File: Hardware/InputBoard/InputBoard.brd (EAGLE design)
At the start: 41.9 x 30.1 mm, 8 parts, among them IC1 LM358N

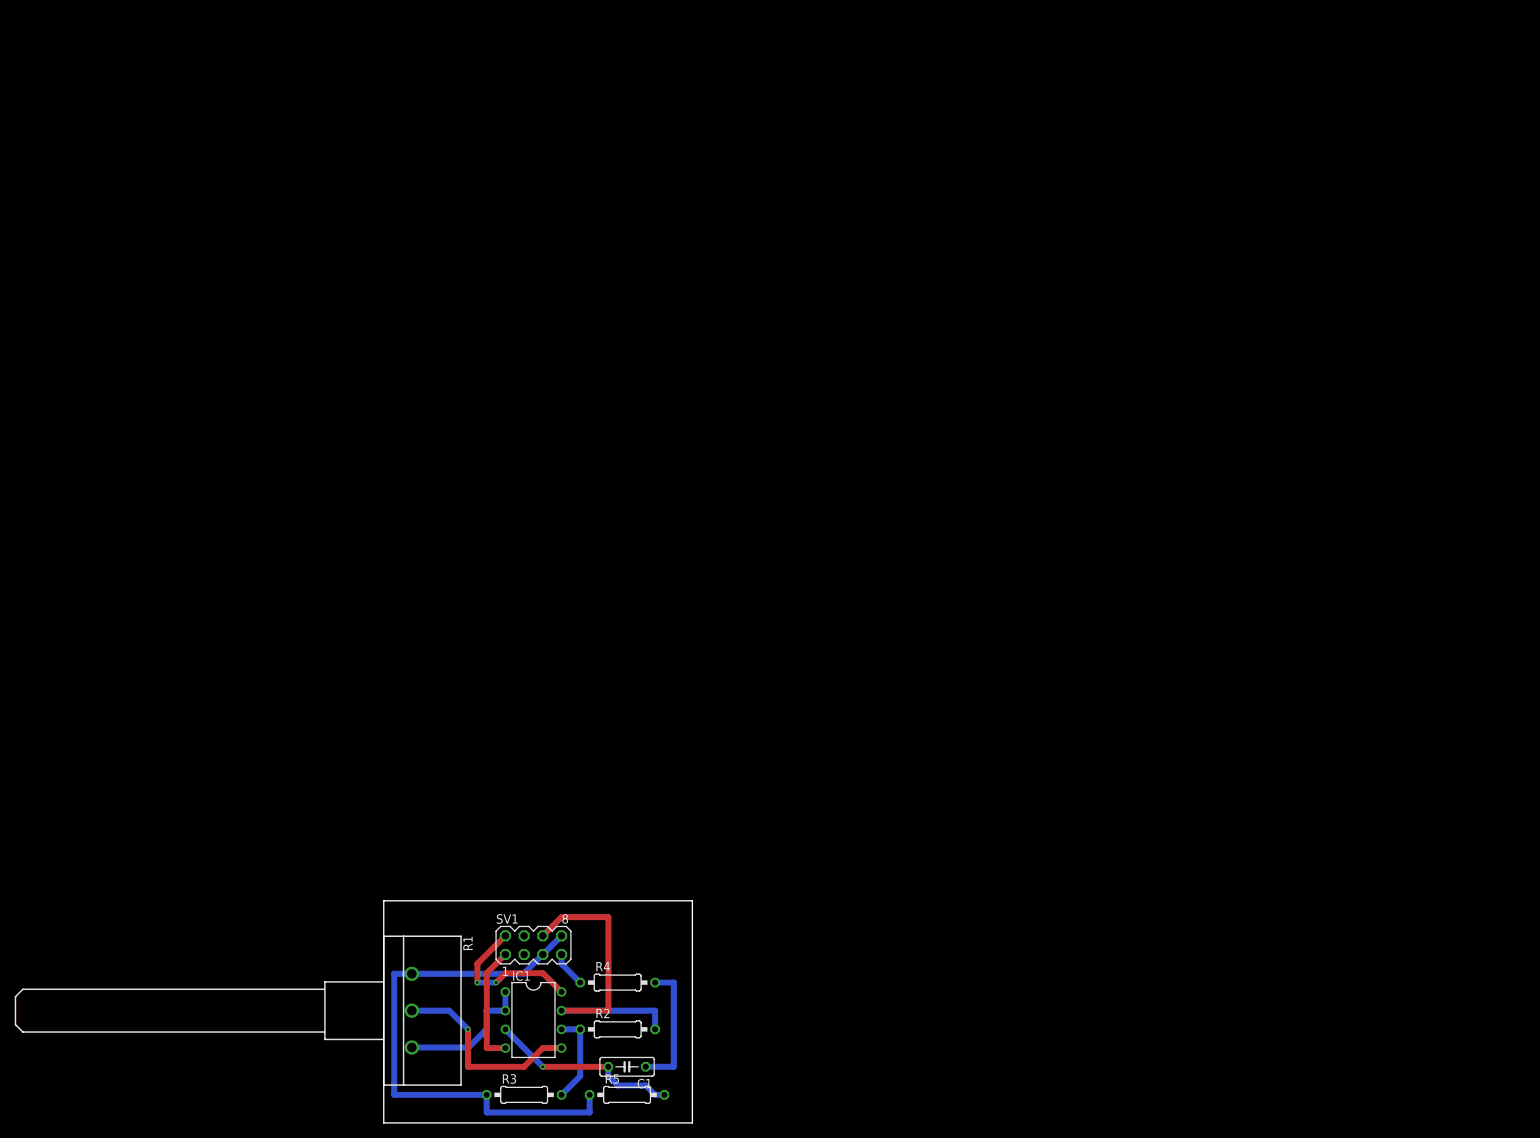
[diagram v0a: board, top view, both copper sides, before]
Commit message: InputBoard überarbeitet, pinout bereitgestellt
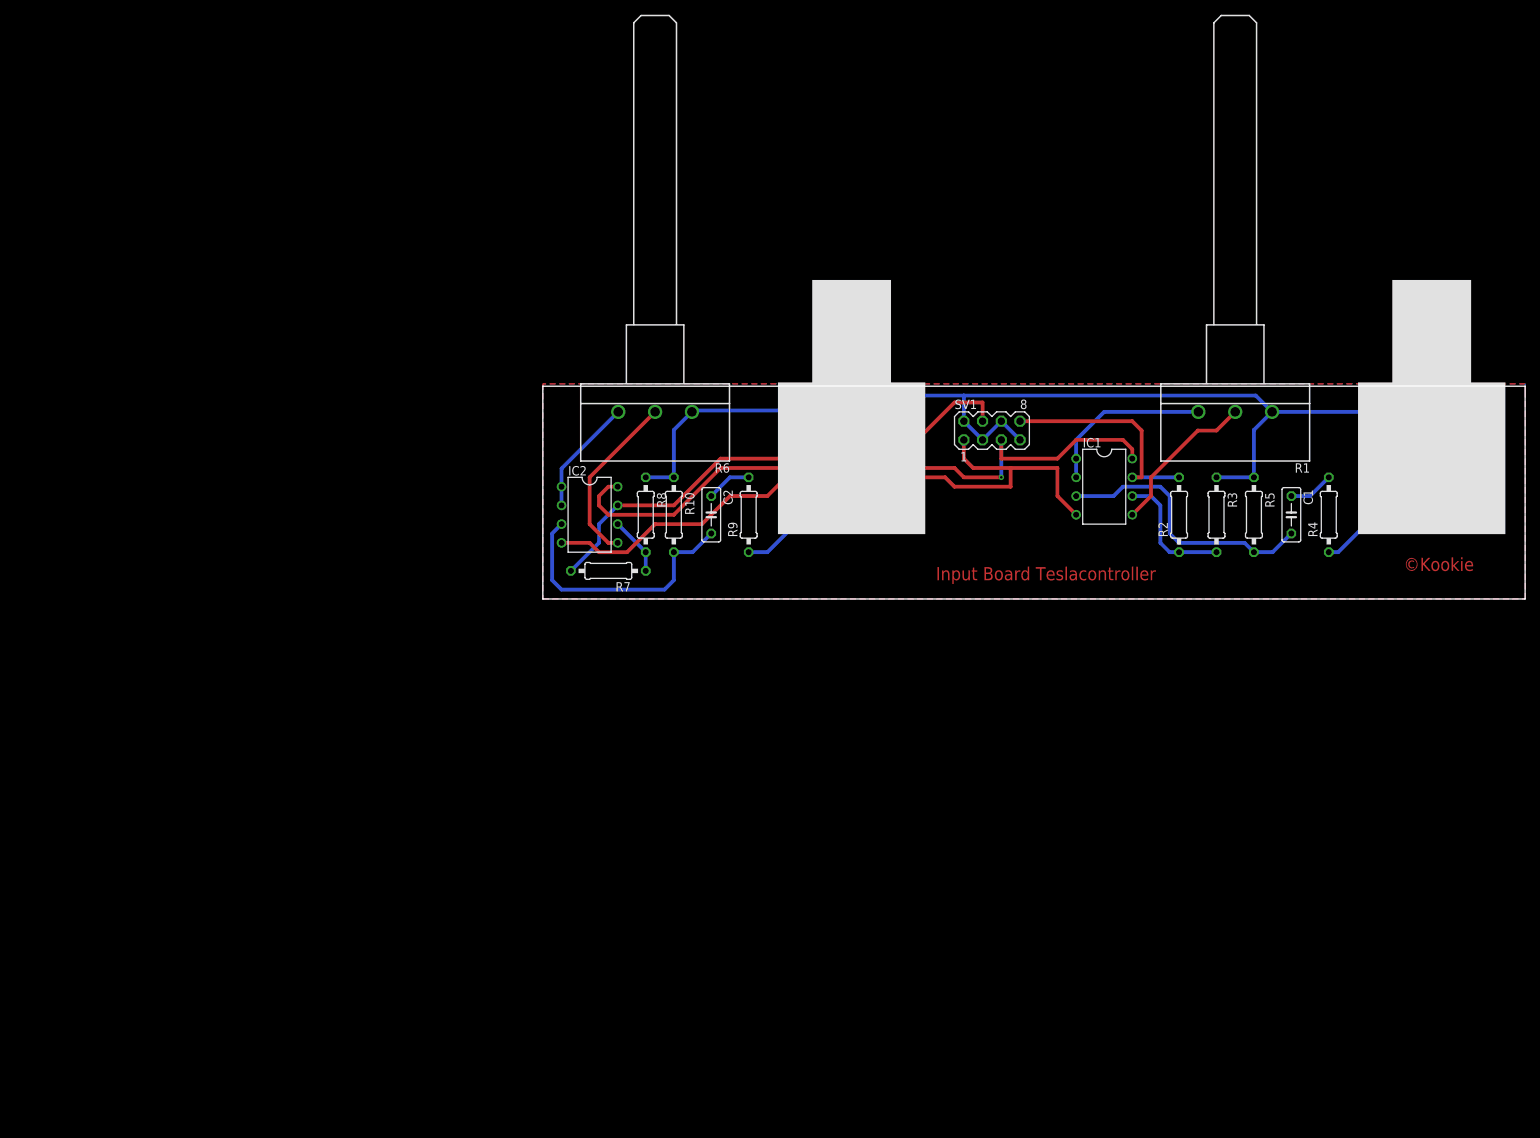
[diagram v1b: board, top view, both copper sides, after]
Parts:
- added C2: 0.001u, rcl:C050-025X075
- added IC2: LM358N, linear:DIL08
- added R10: 1M8, rcl:0207/10
- added R6: (no value), pot:CIP20C-6MM
- added R7: 200k, rcl:0207/10
- added R8: 10k, rcl:0207/10
- added R9: 100k, rcl:0207/10
- added U$1, U$2: (no value), EBS63P:EBS63P
- moved R1 138.2 mm to (115.6, 96.5), turned to 180 degrees
- moved R3 122.6 mm to (113.0, 82.5), turned to 270 degrees
- moved C1 117.2 mm to (123.2, 82.5), turned to 270 degrees
- moved R5 115.9 mm to (118.1, 82.5), turned to 270 degrees
- moved R4 115.5 mm to (128.3, 82.5), turned to 90 degrees
- moved IC1 106.0 mm to (97.8, 86.4)
- moved R2 103.4 mm to (108.0, 82.5), turned to 90 degrees
- moved SV1 93.5 mm to (82.5, 94.0)
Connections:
- removed net IN: R4.1, SV1.7
- removed net OUT: IC1.7, R2.2, SV1.6
- new net N$10: C2.1, R9.2
- new net N$11: R9.1, U$2.P$2
- new net N$12: R4.1, U$1.P$2
- new net N$6: IC2.1, IC2.2, R6.E
- new net N$7: IC2.5, R6.S
- new net N$8: IC2.6, R7.1, R8.2
- new net N$9: C2.2, IC2.3, R10.2
- new net OUT1: IC1.7, R2.2, SV1.8
- new net OUT2: IC2.7, R7.2, SV1.4
- net GND: now also R10.1, R6.A, R8.1, SV1.2, SV1.3, SV1.6, SV1.7, U$1.P$1, U$2.P$1; no longer SV1.5, SV1.8
- net V+: now also IC2.8, SV1.5; no longer SV1.2
- net V-: now also IC2.4
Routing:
- net V-: track 16.3 -> 91.9 mm
- net V+: track 20.9 -> 90.9 mm, vias 2 -> 1
- net OUT2: track 0.00 -> 69.4 mm
- net GND: track 72.6 -> 137.5 mm
- net OUT: track 44.2 -> 0.00 mm
- net N$9: track 0.00 -> 35.7 mm
- net OUT1: track 0.00 -> 31.0 mm
- net N$7: track 0.00 -> 23.8 mm
- net N$6: track 0.00 -> 15.9 mm
- net N$5: track 17.8 -> 6.13 mm
- net N$4: track 26.0 -> 37.4 mm, vias 1 -> 0
- net N$11: track 0.00 -> 10.8 mm
- net N$12: track 0.00 -> 9.77 mm
- net N$8: track 0.00 -> 7.93 mm
- net N$2: track 27.5 -> 21.2 mm, vias 1 -> 0
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- added copper zone on layer 1, net GND
- added copper zone on layer 16, net GND
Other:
- board size 41.9 x 30.1 mm -> 133.3 x 28.9 mm
- board text added: "Input Board Teslacontroller"
- board text added: "©Kookie"

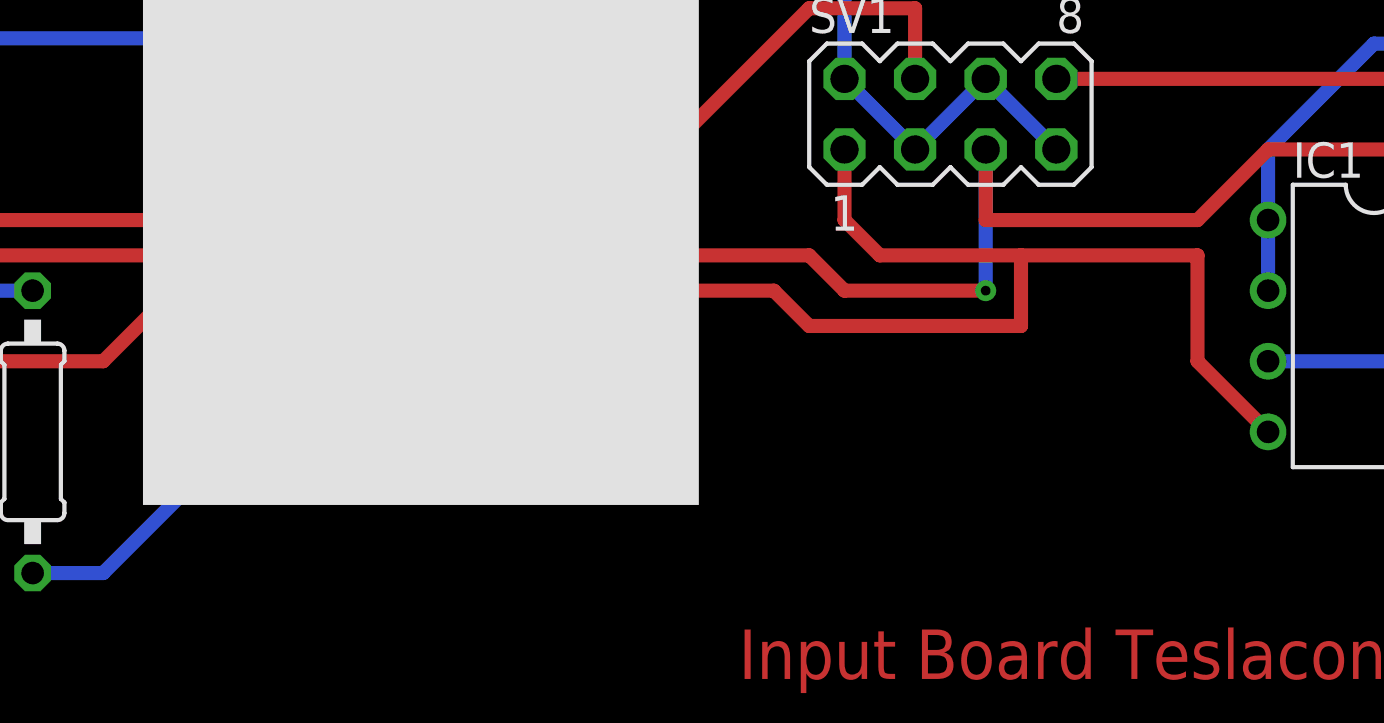
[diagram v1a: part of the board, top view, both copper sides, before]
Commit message: Letzte Änderungen an Netzteil, OP und IP Board
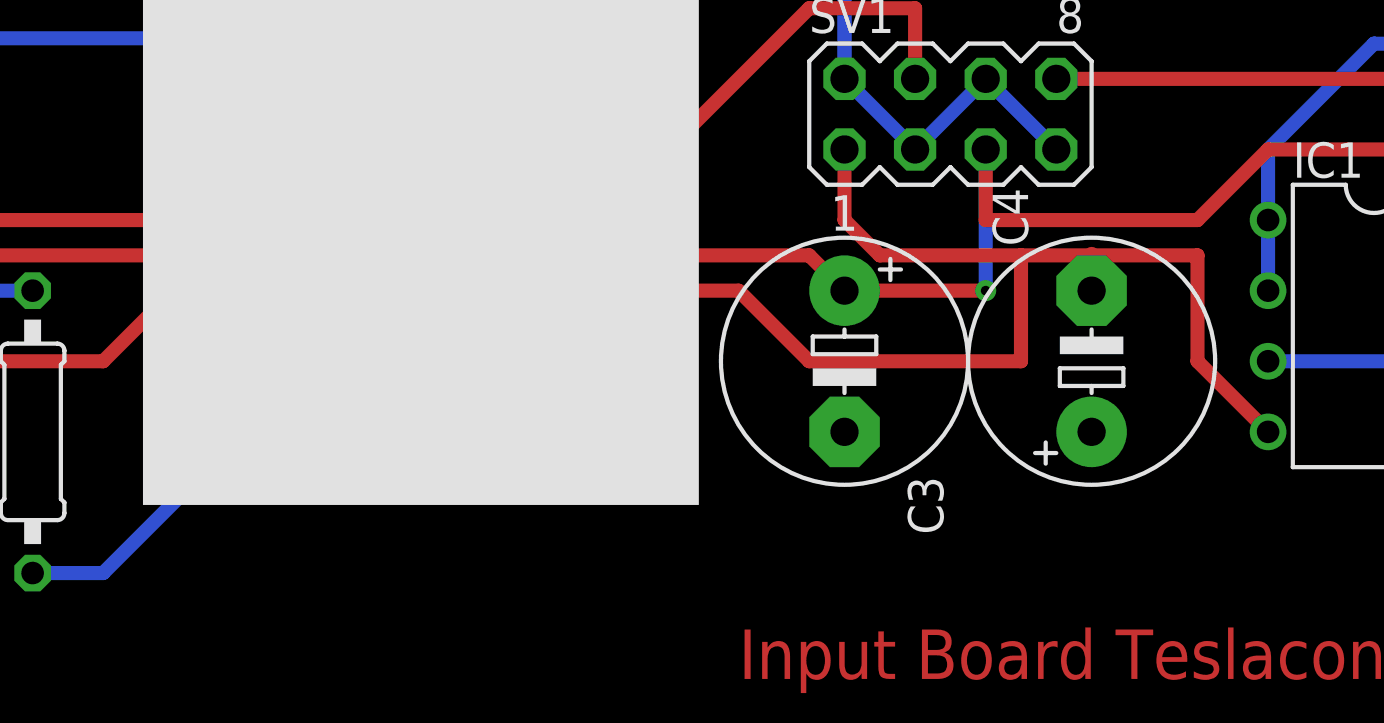
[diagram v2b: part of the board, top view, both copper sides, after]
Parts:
- added C3, C4: (no value), rcl:E5-8,5
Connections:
- net GND: now also C3.-, C4.+
- net V+: now also C3.+
- net V-: now also C4.-
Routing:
- net V-: track 91.9 -> 95.0 mm
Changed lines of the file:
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@@
 <?xml version="1.0" encoding="utf-8"?>
 <!DOCTYPE eagle SYSTEM "eagle.dtd">
-<eagle version="9.4.1">
+<eagle version="9.4.0">
 <drawing>
 <settings>
@@
 <element name="U$1" library="EBS63P" package="EBS63P" value="" x="142.24" y="96.52" smashed="yes" rot="R270"/>
 <element name="U$2" library="EBS63P" package="EBS63P" value="" x="63.5" y="96.52" smashed="yes" rot="R270"/>
+<element name="C3" library="rcl" library_urn="urn:adsk.eagle:library:334" package="E5-8,5" package3d_urn="urn:adsk.eagle:package:23374/1" value="" x="78.74" y="85.09" smashed="yes" rot="R270">
+<attribute name="NAME" x="81.026" y="80.9498" size="1.27" layer="25" ratio="10" rot="R270"/>
+<attribute name="SPICEPREFIX" value="C" x="78.74" y="85.09" size="1.778" layer="27" rot="R270" display="off"/>
+<attribute name="VALUE" x="75.7174" y="87.6046" size="1.27" layer="27" ratio="10" rot="R270"/>
+</element>
+<element name="C4" library="rcl" library_urn="urn:adsk.eagle:library:334" package="E5-8,5" package3d_urn="urn:adsk.eagle:package:23374/1" value="" x="87.63" y="85.09" smashed="yes" rot="R90">
+<attribute name="NAME" x="85.344" y="89.2302" size="1.27" layer="25" ratio="10" rot="R90"/>
+<attribute name="SPICEPREFIX" value="C" x="87.63" y="85.09" size="1.778" layer="27" rot="R90" display="off"/>
+<attribute name="VALUE" x="90.6526" y="82.5754" size="1.27" layer="27" ratio="10" rot="R90"/>
+</element>
 </elements>
 <signals>
@@
 <via x="83.82" y="87.63" extent="1-16" drill="0.35" shape="octagon"/>
 <wire x1="83.82" y1="87.63" x2="83.82" y2="92.71" width="0.508" layer="16"/>
+<contactref element="C3" pad="+"/>
 </signal>
 <signal name="V-">
@@
 <wire x1="80.01" y1="88.9" x2="78.74" y2="90.17" width="0.508" layer="1"/>
 <wire x1="78.74" y1="90.17" x2="78.74" y2="92.71" width="0.508" layer="1"/>
-<wire x1="91.44" y1="88.9" x2="85.09" y2="88.9" width="0.508" layer="1"/>
+<wire x1="91.44" y1="88.9" x2="87.63" y2="88.9" width="0.508" layer="1"/>
+<wire x1="87.63" y1="88.9" x2="85.09" y2="88.9" width="0.508" layer="1"/>
 <wire x1="85.09" y1="88.9" x2="80.01" y2="88.9" width="0.508" layer="1"/>
 <wire x1="24.13" y1="78.74" x2="27.94" y2="78.74" width="0.508" layer="1"/>
@@
 <wire x1="46.99" y1="85.09" x2="52.07" y2="85.09" width="0.508" layer="1"/>
 <wire x1="52.07" y1="85.09" x2="54.61" y2="87.63" width="0.508" layer="1"/>
-<wire x1="54.61" y1="87.63" x2="76.2" y2="87.63" width="0.508" layer="1"/>
-<wire x1="76.2" y1="87.63" x2="77.47" y2="86.36" width="0.508" layer="1"/>
-<wire x1="77.47" y1="86.36" x2="85.09" y2="86.36" width="0.508" layer="1"/>
-<wire x1="85.09" y1="86.36" x2="85.09" y2="88.9" width="0.508" layer="1"/>
+<wire x1="54.61" y1="87.63" x2="74.93" y2="87.63" width="0.508" layer="1"/>
+<wire x1="74.93" y1="87.63" x2="77.47" y2="85.09" width="0.508" layer="1"/>
+<wire x1="77.47" y1="85.09" x2="85.09" y2="85.09" width="0.508" layer="1"/>
+<wire x1="85.09" y1="85.09" x2="85.09" y2="88.9" width="0.508" layer="1"/>
 <wire x1="36.83" y1="81.28" x2="43.18" y2="81.28" width="0.508" layer="1"/>
+<contactref element="C4" pad="-"/>
+<wire x1="87.63" y1="87.63" x2="87.63" y2="88.9" width="0.6096" layer="1"/>
 </signal>
 <signal name="N$1">
@@
 <vertex x="154.94" y="100.33"/>
 </polygon>
+<contactref element="C3" pad="-"/>
+<contactref element="C4" pad="+"/>
 </signal>
 <signal name="N$3">

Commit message: Minor Board Fixes
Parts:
- moved C3 76.9 mm to (57.7, 11.1)
- moved C4 76.9 mm to (66.6, 11.1)
- moved C1 74.0 mm to (102.2, 11.6)
- moved C2 74.0 mm to (23.4, 11.6)
- moved IC1 74.0 mm to (76.8, 15.4)
- moved IC2 74.0 mm to (6.94, 11.6)
- moved R1 74.0 mm to (94.6, 25.5)
- moved R10 74.0 mm to (18.4, 11.6)
- moved R2 74.0 mm to (87.0, 11.6)
- moved R3 74.0 mm to (92.0, 11.6)
- moved R4 74.0 mm to (107.3, 11.6)
- moved R5 74.0 mm to (97.1, 11.6)
- moved R6 74.0 mm to (15.8, 25.5)
- moved R7 74.0 mm to (9.48, 3.93)
- moved R8 74.0 mm to (14.6, 11.6)
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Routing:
- net V-: track 95.0 -> 102.2 mm
- net V+: track 90.9 -> 93.4 mm
